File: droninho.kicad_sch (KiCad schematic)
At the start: 19 parts, among them J1 M1, J2 M1, J3 M1, J4 M1, J5 Conn_01x02_Pin, Q1 SI2300, Q2 SI2300, Q3 SI2300, Q4 SI2300, U1 ESP32 Dev Kit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

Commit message: Electrical part finished
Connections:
- net +3.3V: now also U1.1 (VIN)
- no-connect marks 6 -> 27
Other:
- moved on the sheet: U1

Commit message: Readme added
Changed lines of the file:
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@@
 	)
 	(global_label "SCL"
-		(shape input)
+		(shape output)
 		(at 228.6 88.9 0)
 		(fields_autoplaced yes)
@@
 	)
 	(global_label "SDA"
-		(shape input)
+		(shape bidirectional)
 		(at 151.892 98.044 0)
 		(fields_autoplaced yes)
@@
 		)
 		(property "Intersheetrefs" "${INTERSHEET_REFS}"
-			(at 158.4453 98.044 0)
+			(at 159.5566 98.044 0)
 			(effects
 				(font
@@
 	)
 	(global_label "SDA"
-		(shape input)
+		(shape bidirectional)
 		(at 228.6 96.52 0)
 		(fields_autoplaced yes)
@@
 		)
 		(property "Intersheetrefs" "${INTERSHEET_REFS}"
-			(at 235.1533 96.52 0)
-			(effects
-				(font
+			(at 236.2646 96.52 0)
+			(effects
+				(font

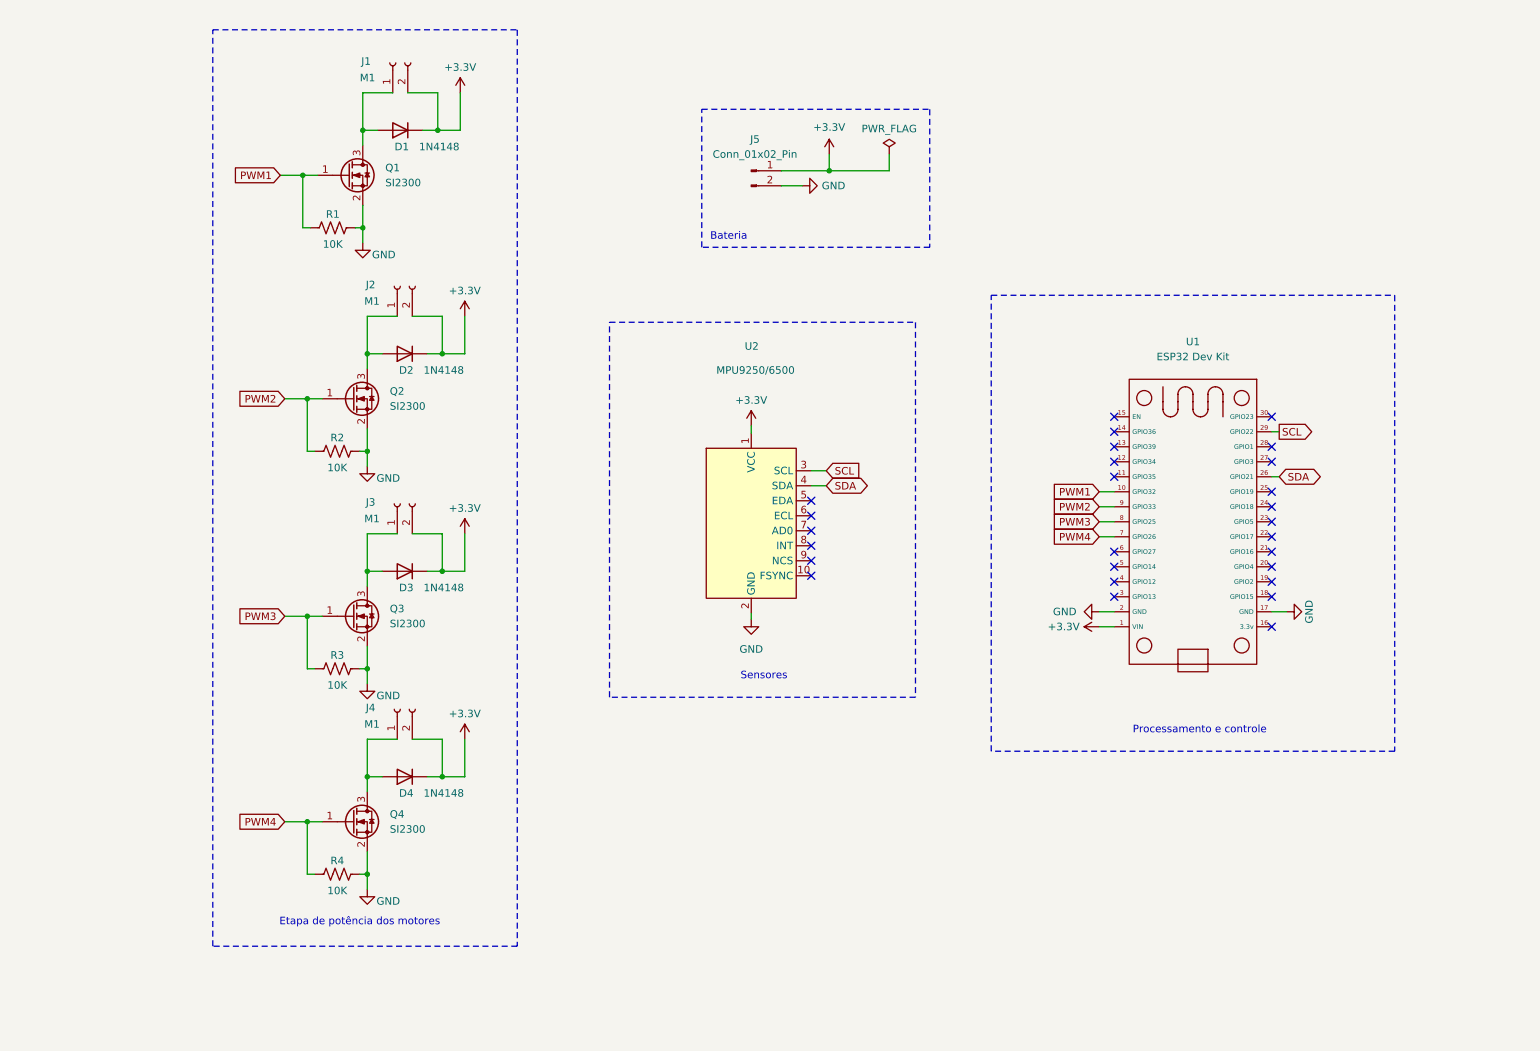
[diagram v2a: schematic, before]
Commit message: add nets to schematic
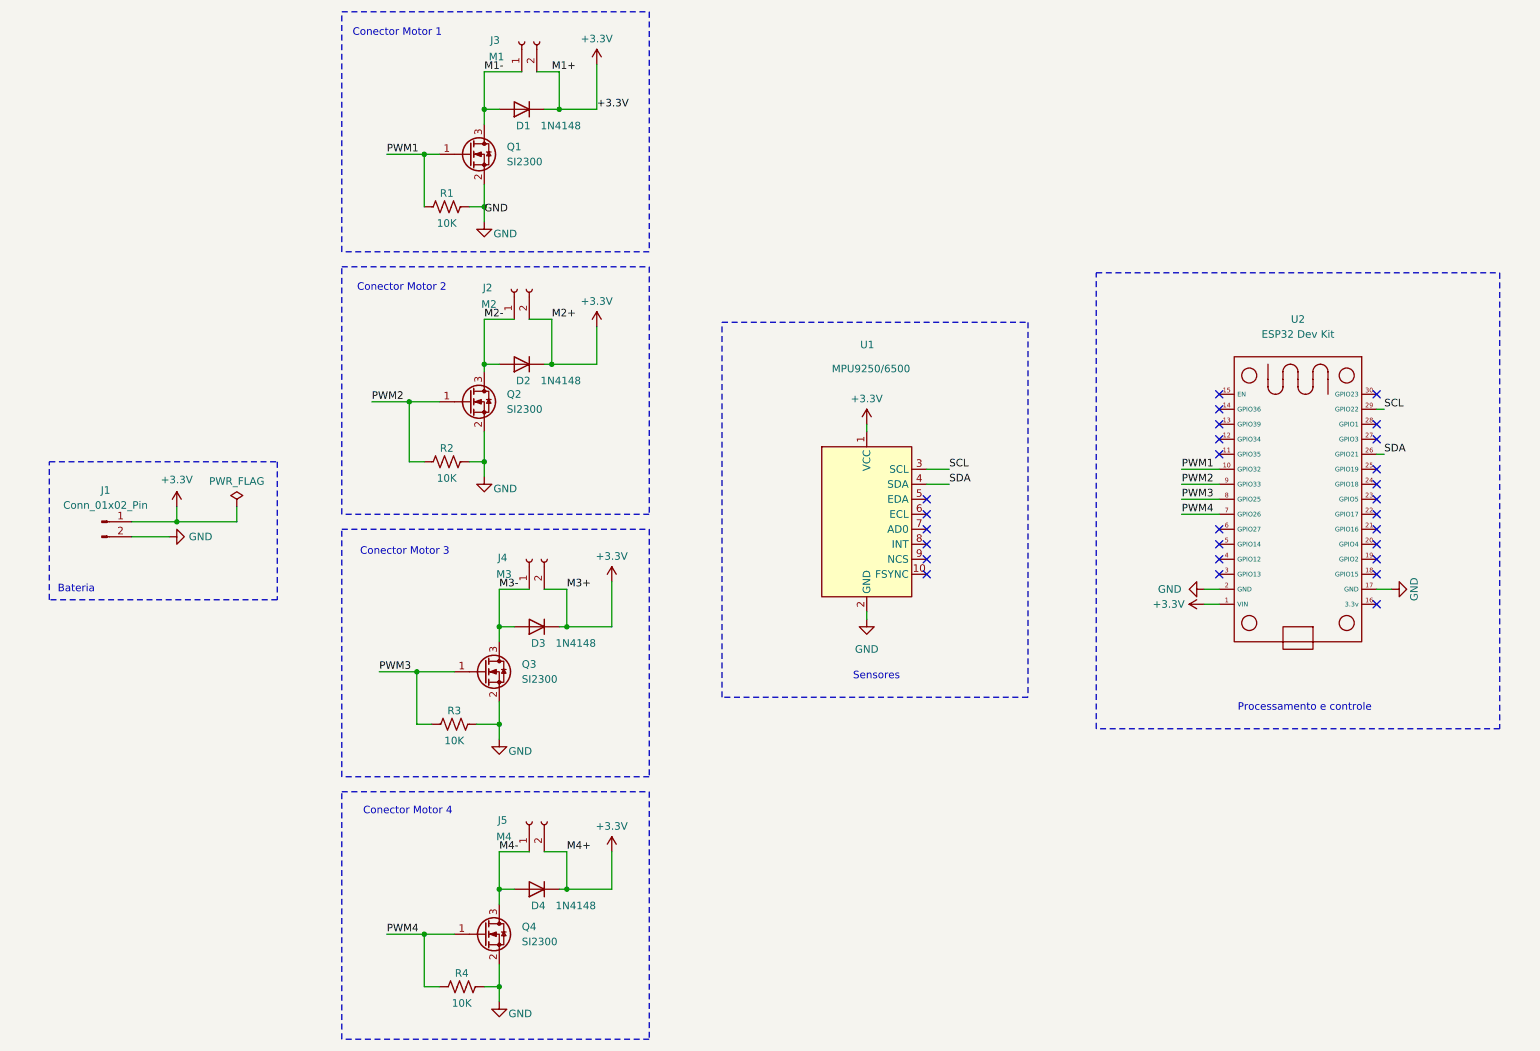
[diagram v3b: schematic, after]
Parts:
- J2: value M1 -> M2
- J4: renamed from J3; value M1 -> M3
- J5: renamed from J4; value M1 -> M4
- renumbered J5 to J1, J1 to J3, U2 to U1, U1 to U2
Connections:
- net M1-: now reaches D1.2 (A), J3.1 (Pin_1), Q1.3 (D)
- net M2-: now reaches D2.2 (A), J2.1 (Pin_1), Q2.3 (D)
- net M3-: now reaches D3.2 (A), J4.1 (Pin_1), Q3.3 (D)
- net M4-: now reaches D4.2 (A), J5.1 (Pin_1), Q4.3 (D)
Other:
- note added: "Conector Motor 1"
- note added: "Conector Motor 2"
- note added: "Conector Motor 3"
- note added: "Conector Motor 4"
- note removed: "Etapa de potência dos motores"
- moved on the sheet: D1, D2, D3, D4, J1, J2, J3, J4, J5, Q1, Q2, Q3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

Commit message: ERC OK!
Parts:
- U1: footprint MPU-9250-6500:MPU-9250-6500 -> Library:MPU-9250-6500
- U2: footprint esp32_30_38pin:ESP32_30pin -> Library:ESP32_30pin
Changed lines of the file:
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@@
+	)
+	(junction
+		(at 38.1 106.68)
+		(diameter 0)
+		(color 0 0 0 0)
 	)
 	(junction
@@
 	(wire
 		(pts
+			(xy 38.1 106.68) (xy 40.64 106.68)
+		)
+		(stroke
+			(width 0)
+			(type default)
+		)
+	)
+	(wire
+		(pts
 			(xy 96.52 124.46) (xy 96.52 121.92)
 		)
@@
 	(wire
 		(pts
+			(xy 52.07 113.03) (xy 38.1 113.03)
+		)
+		(stroke
+			(width 0)
+			(type default)
+		)
+	)
+	(wire
+		(pts
 			(xy 86.36 182.88) (xy 83.82 182.88)
 		)
@@
 	(wire
 		(pts
+			(xy 52.07 111.76) (xy 52.07 113.03)
+		)
+		(stroke
+			(width 0)
+			(type default)
+		)
+	)
+	(wire
+		(pts
 			(xy 113.03 77.47) (xy 105.41 77.47)
 		)
@@
 	(wire
 		(pts
+			(xy 38.1 113.03) (xy 38.1 106.68)
+		)
+		(stroke
+			(width 0)
+			(type default)
+		)
+	)
+	(wire
+		(pts
 			(xy 91.44 93.98) (xy 93.98 93.98)
 		)
@@
 	(wire
 		(pts
-			(xy 34.29 106.68) (xy 40.64 106.68)
+			(xy 34.29 106.68) (xy 38.1 106.68)
 		)
 		(stroke
@@
 			)
 		)
-		(property "Footprint" "MPU-9250-6500:MPU-9250-6500"
+		(property "Footprint" "Library:MPU-9250-6500"
 			(at 160.274 79.756 0)
 			(effects
@@
 				(path "/50215636-8ce2-4b01-ade7-3715bffabe9d"
 					(reference "D3")
+					(unit 1)
+				)
+			)
+		)
+	)
+	(symbol
+		(lib_id "power:PWR_FLAG")
+		(at 52.07 111.76 0)
+		(unit 1)
+		(exclude_from_sim no)
+		(in_bom yes)
+		(on_board yes)
+		(dnp no)
+		(fields_autoplaced yes)
+		(property "Reference" "#FLG02"
+			(at 52.07 109.855 0)
+			(effects
+				(font
+					(size 1.27 1.27)
+				)
+				(hide yes)
+			)
+		)
+		(property "Value" "PWR_FLAG"
+			(at 52.07 107.442 0)
+			(effects
+				(font
+					(size 1.27 1.27)
+				)
+			)
+		)
+		(property "Footprint" ""
+			(at 52.07 111.76 0)
+			(effects
+				(font
+					(size 1.27 1.27)
+				)
+				(hide yes)
+			)
+		)
+		(property "Datasheet" "~"
+			(at 52.07 111.76 0)
+			(effects
+				(font
+					(size 1.27 1.27)
+				)
+				(hide yes)
+			)
+		)
+		(property "Description" "Special symbol for telling ERC where power comes from"
+			(at 52.07 111.76 0)
+			(effects
+				(font
+					(size 1.27 1.27)
+				)
+				(hide yes)
+			)
+		)
+		(pin "1"
+		)
+		(instances
+			(project "droninho"
+				(path "/50215636-8ce2-4b01-ade7-3715bffabe9d"
+					(reference "#FLG02")
 					(unit 1)
 				)
@@
 			)
 		)
-		(property "Footprint" "esp32_30_38pin:ESP32_30pin"
+		(property "Footprint" "Library:ESP32_30pin"
 			(at 231.775 73.66 90)
 			(effects

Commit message: ERC Done
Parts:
- removed U1: MPU9250/6500, Library:MPU-9250-6500, symbol MPU-9250-6500:MPU-9250-6500
- removed U2: ESP32 Dev Kit, Library:ESP32_30pin, symbol esp32_30pin:ESP32_30Pin
- added U1: ESP32 Dev Kit, Library:ESP32_30pin, symbol Library:ESP32_30Pin
- added U3: MPU9250/6500, Library:MPU-9250-6500, symbol Library:MPU-9250-6500
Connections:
- net +3.3V: now also U1.1 (VIN), U3.1 (VCC)
- net GND: now also U1.17 (GND), U1.2 (GND), U3.2 (GND)
- net PWM1: now also U1.10 (GPIO32)
- net PWM2: now also U1.9 (GPIO33)
- net PWM3: now also U1.8 (GPIO25)
- net PWM4: now also U1.7 (GPIO26)
- net SCL: now also U1.29 (GPIO22), U3.3 (SCL)
- net SDA: now also U1.26 (GPIO21), U3.4 (SDA)
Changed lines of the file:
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@@
-		)
-	)
-	(label "M2+"
-		(at 105.41 69.85 0)
-		(effects
-			(font
-				(size 1.27 1.27)
-			)
-			(justify left bottom)
-		)
-	)
-	(label "M1+"
-		(at 105.41 27.94 0)
-		(effects
-			(font
-				(size 1.27 1.27)
-			)
-			(justify left bottom)
 		)
 	)
@@
 		)
 	)
-	(label "M3+"
-		(at 107.95 115.57 0)
-		(effects
-			(font
-				(size 1.27 1.27)
-			)
-			(justify left bottom)
-		)
-	)
 	(label "PWM4"
 		(at 212.09 102.87 0)
@@
 		)
 	)
-	(label "M4+"
-		(at 107.95 160.02 0)
-		(effects
-			(font
-				(size 1.27 1.27)
-			)
-			(justify left bottom)
-		)
-	)
 	(label "PWM1"
 		(at 212.09 95.25 0)
@@
 	)
 	(symbol
+		(lib_id "Library:MPU-9250-6500")
+		(at 160.02 96.52 0)
+		(unit 1)
+		(exclude_from_sim no)
+		(in_bom yes)
+		(on_board yes)
+		(dnp no)
+		(fields_autoplaced yes)
+		(property "Reference" "U3"
+			(at 149.86 102.8699 0)
+			(effects
+				(font
+					(size 1.27 1.27)
+				)
+				(justify right)
+			)
+		)
+		(property "Value" "MPU9250/6500"
+			(at 149.86 105.4099 0)
+			(effects
+				(font
+					(size 1.27 1.27)
+				)
+				(justify right)
+			)
+		)
+		(property "Footprint" "Library:MPU-9250-6500"
+			(at 160.274 79.756 0)
+			(effects
+				(font
+					(size 1.27 1.27)
+				)
+				(hide yes)
+			)
+		)
+		(property "Datasheet" ""
+			(at 160.02 96.52 0)
+			(effects
+				(font
+					(size 1.27 1.27)
+				)
+				(hide yes)
+			)
+		)
+		(property "Description" ""
+			(at 160.02 96.52 0)
+			(effects
+				(font
+					(size 1.27 1.27)
+				)
+				(hide yes)
+			)
+		)
+		(pin "4"
+		)
+		(pin "6"
+		)
+		(pin "2"
+		)
+		(pin "3"
+		)
+		(pin "10"
+		)
+		(pin "8"
+		)
+		(pin "7"
+		)
+		(pin "1"
+		)
+		(pin "9"
+		)
+		(pin "5"
+		)
+		(instances
+			(project ""
+				(path "/50215636-8ce2-4b01-ade7-3715bffabe9d"
+					(reference "U3")
+					(unit 1)
+				)
+			)
+		)
+	)
+	(symbol
 		(lib_id "Device:R_US")
 		(at 87.63 93.98 90)
@@
 				(path "/50215636-8ce2-4b01-ade7-3715bffabe9d"
 					(reference "#PWR03")
-					(unit 1)
-				)
-			)
-		)
-	)
-	(symbol
-		(lib_id "MPU-9250-6500:MPU-9250-6500")
-		(at 160.02 96.52 0)
-		(unit 1)
-		(exclude_from_sim no)
-		(in_bom yes)
-		(on_board yes)
-		(dnp no)
-		(property "Reference" "U1"
-			(at 160.02 74.168 0)
-			(effects
-				(font
-					(size 1.27 1.27)
-				)
-				(justify right)
-			)
-		)
-		(property "Value" "MPU9250/6500"
-			(at 166.116 78.232 0)
-			(effects
-				(font
-					(size 1.27 1.27)
-				)
-				(justify right)
-			)
-		)
-		(property "Footprint" "Library:MPU-9250-6500"
-			(at 160.274 79.756 0)
-			(effects
-				(font
-					(size 1.27 1.27)
-				)
-				(hide yes)
-			)
-		)
-		(property "Datasheet" ""
-			(at 160.02 96.52 0)
-			(effects
-				(font
-					(size 1.27 1.27)
-				)
-				(hide yes)
-			)
-		)
-		(property "Description" ""
-			(at 160.02 96.52 0)
-			(effects
-				(font
-					(size 1.27 1.27)
-				)
-				(hide yes)
-			)
-		)
-		(pin "4"
-		)
-		(pin "2"
-		)
-		(pin "3"
-		)
-		(pin "6"
-		)
-		(pin "1"
-		)
-		(pin "7"
-		)
-		(pin "8"
-		)
-		(pin "5"
-		)
-		(pin "10"
-		)
-		(pin "9"
-		)
-		(instances
-			(project ""
-				(path "/50215636-8ce2-4b01-ade7-3715bffabe9d"
-					(reference "U1")
 					(unit 1)
 				)
@@
 	)
 	(symbol
-		(lib_id "esp32_30pin:ESP32_30Pin")
-		(at 231.775 100.33 270)
-		(unit 1)
-		(exclude_from_sim no)
-		(in_bom yes)
-		(on_board yes)
-		(dnp no)
-		(fields_autoplaced yes)
-		(property "Reference" "U2"
-			(at 231.775 69.85 90)
-			(effects
-				(font
-					(size 1.27 1.27)
-				)
-			)
-		)
-		(property "Value" "ESP32 Dev Kit"
-			(at 231.775 72.39 90)
-			(effects
-				(font
-					(size 1.27 1.27)
-				)
-			)
-		)
-		(property "Footprint" "Library:ESP32_30pin"
-			(at 231.775 73.66 90)
-			(effects
-				(font
-					(size 1.27 1.27)
-					(color 194 194 0 1)
-				)
-				(hide yes)
-			)
-		)
-		(property "Datasheet" ""
-			(at 231.775 100.33 0)
-			(effects
-				(font
-					(size 1.27 1.27)
-				)
-				(hide yes)
-			)
-		)
-		(property "Description" ""
-			(at 231.775 100.33 0)
-			(effects
-				(font
-					(size 1.27 1.27)
-				)
-				(hide yes)
-			)
-		)
-		(pin "19"
-		)
-		(pin "17"
-		)
-		(pin "22"
-		)
-		(pin "30"
-		)
-		(pin "15"
-		)
-		(pin "29"
-		)
-		(pin "28"
-		)
-		(pin "13"
-		)
-		(pin "21"
-		)
-		(pin "5"
-		)
-		(pin "7"
-		)
-		(pin "11"
-		)
-		(pin "2"
-		)
-		(pin "25"
-		)
-		(pin "16"
-		)
-		(pin "1"
-		)
-		(pin "12"
-		)
-		(pin "23"
-		)
-		(pin "24"
-		)
-		(pin "9"
-		)
-		(pin "20"
-		)
-		(pin "14"
-		)
-		(pin "10"
-		)
-		(pin "26"
-		)
-		(pin "4"
-		)
-		(pin "8"
-		)
-		(pin "3"
-		)
-		(pin "18"
-		)
-		(pin "6"
-		)
-		(pin "27"
-		)
-		(instances
-			(project ""
-				(path "/50215636-8ce2-4b01-ade7-3715bffabe9d"
-					(reference "U2")
-					(unit 1)
-				)
-			)
-		)
-	)
-	(symbol
 		(lib_id "power:+3.3V")
 		(at 215.9 118.11 90)
@@
 					(unit 1)
 				)
+			)
+		)
+	)
+	(symbol
+		(lib_id "Library:ESP32_30Pin")
+		(at 231.775 100.33 270)
+		(unit 1)
+		(exclude_from_sim no)
+		(in_bom yes)
+		(on_board yes)
+		(dnp no)
+		(fields_autoplaced yes)
+		(property "Reference" "U1"
+			(at 231.775 71.12 90)
+			(effects
+				(font
+					(size 1.27 1.27)
+				)
+			)
+		)
+		(property "Value" "ESP32 Dev Kit"
+			(at 231.775 73.66 90)
+			(effects
+				(font
+					(size 1.27 1.27)
+				)
+			)
+		)
+		(property "Footprint" "Library:ESP32_30pin"
+			(at 231.775 73.66 90)
+			(effects
+				(font
+					(size 1.27 1.27)
+					(color 194 194 0 1)
+				)
+				(hide yes)
+			)
+		)
+		(property "Datasheet" ""
+			(at 231.775 100.33 0)
+			(effects
+				(font
+					(size 1.27 1.27)
+				)
+				(hide yes)
+			)
+		)
+		(property "Description" ""
+			(at 231.775 100.33 0)
+			(effects
+				(font
+					(size 1.27 1.27)
+				)
+				(hide yes)
+			)
+		)
+		(pin "13"
+		)
+		(pin "30"
+		)
+		(pin "15"
+		)
+		(pin "29"
+		)
+		(pin "14"
+		)
+		(pin "28"
+		)
+		(pin "25"
+		)
+		(pin "23"
+		)
+		(pin "10"
+		)
+		(pin "18"
+		)
+		(pin "3"
+		)
+		(pin "20"
+		)
+		(pin "12"
+		)
+		(pin "27"
+		)
+		(pin "26"
+		)
+		(pin "22"
+		)
+		(pin "7"
+		)
+		(pin "8"
+		)
+		(pin "6"
+		)
+		(pin "9"
+		)
+		(pin "21"
+		)
+		(pin "5"
+		)
+		(pin "11"
+		)
+		(pin "24"
+		)
+		(pin "19"
+		)
+		(pin "4"
+		)
+		(pin "2"
+		)
+		(pin "17"
+		)
+		(pin "1"
+		)
+		(pin "16"
+		)
+		(instances
+			(project ""
+				(path "/50215636-8ce2-4b01-ade7-3715bffabe9d"
+					(reference "U1")
+					(unit 1)
+				)

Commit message: Footprints checked.
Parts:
- D1, D2, D3, D4: footprint Diode_SMD:D_0201_0603Metric -> Diode_SMD:D_SOD-110
- J1: footprint Connector:JWT_A3963_1x02_P3.96mm_Vertical -> Connector_JST:JST_EH_B2B-EH-A_1x02_P2.50mm_Vertical
- J2, J3, J4, J5: footprint Connector_AMASS:AMASS_XT30UPB-F_1x02_P5.0mm_Vertical -> Connector_JST:JST_PH_B2B-PH-K_1x02_P2.00mm_Vertical
- R1, R2, R3, R4: footprint Resistor_SMD:R_0201_0603Metric -> Resistor_SMD:R_0805_2012Metric_Pad1.20x1.40mm_HandSolder
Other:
- moved on the sheet: R1, R2, R3, R4

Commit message: PCB finalizado.
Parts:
- removed U1: ESP32 Dev Kit, Library:ESP32_30pin, symbol Library:ESP32_30Pin
- added J6, J8: I2C, Connector:FanPinHeader_1x04_P2.54mm_Vertical, symbol Connector:Conn_01x04_Pin
- added J7: TXD0/RXD0, Connector:FanPinHeader_1x04_P2.54mm_Vertical, symbol Connector:Conn_01x04_Pin
- added U2: ESP32 Dev Kit, Library:ESP32_30pin, symbol Library:ESP32_30Pin
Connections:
- net +3.3V: now also J6.3 (Pin_3), J7.3 (Pin_3), J8.3 (Pin_3), U2.1 (VIN)
- net GND: now also J6.4 (Pin_4), J7.4 (Pin_4), J8.4 (Pin_4), U2.17 (GND), U2.2 (GND)
- net PWM1: now also U2.10 (GPIO32)
- net PWM2: now also U2.9 (GPIO33)
- net PWM3: now also U2.8 (GPIO25)
- net PWM4: now also U2.7 (GPIO26)
- net SCL: now also J6.1 (Pin_1), U2.29 (GPIO22)
- net SDA: now also J6.2 (Pin_2), U2.26 (GPIO21)
- new net RXD0: J7.2 (Pin_2), U2.27 (GPIO3)
- new net RXD2: J8.2 (Pin_2), U2.21 (GPIO16)
- new net TXD0: J7.1 (Pin_1), U2.28 (GPIO1)
- new net TXD2: J8.1 (Pin_1), U2.22 (GPIO17)
- no-connect marks 27 -> 23
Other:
- note added: "Conector I2C"
- note added: "Conector TXD0/RXD0"
- note added: "Conector TXD2/RXD2"
- moved on the sheet: D1, D2, D3, D4, J1, J2, J3, J4, J5, Q1, Q2, Q3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

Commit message: Ready for review.
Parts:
- removed U3: MPU9250/6500, Library:MPU-9250-6500, symbol Library:MPU-9250-6500
- added U4: MPU9250/6500, Library:MPU-9250-6500, symbol Library:MPU-9250-6500
- J6, J7, J8: footprint Connector:FanPinHeader_1x04_P2.54mm_Vertical -> Connector_PinHeader_2.54mm:PinHeader_1x04_P2.54mm_Vertical
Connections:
- net +3.3V: now also U4.1 (VCC)
- net GND: now also U4.2 (GND)
- net SCL: now also U4.3 (SCL)
- net SDA: now also U4.4 (SDA)
